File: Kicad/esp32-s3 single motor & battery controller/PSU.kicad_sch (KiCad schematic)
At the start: 73 parts, among them J5 Batt Balance connector, Q1 NMOS,12v, Q2 NMOS, 12v, Q3 NMOS,12v,PPak, Q4 NMOS, 12v, Q5 NMOS, 12v, Q7 NMOS,12v,PPak, U2 AP63203WU, U3 BQ76905RGRR, U4 BQ24780SRUYR

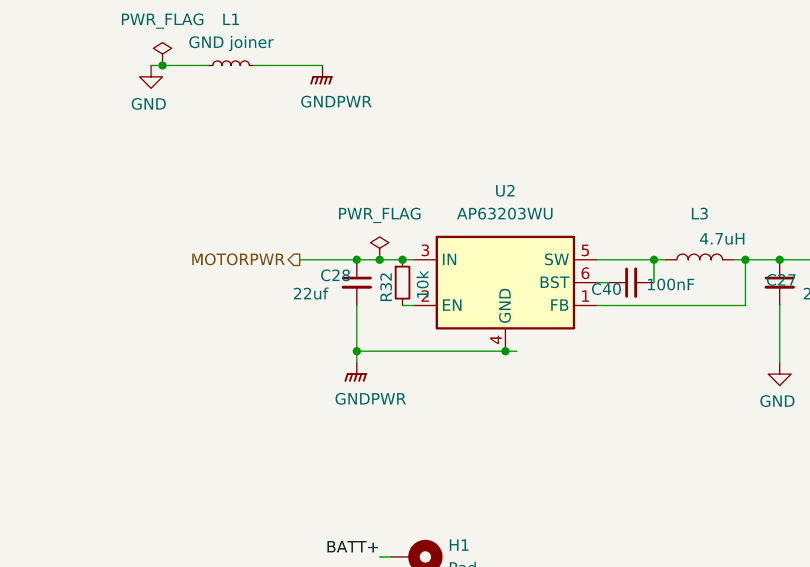
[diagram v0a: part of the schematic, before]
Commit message: Fixing routing issues after change
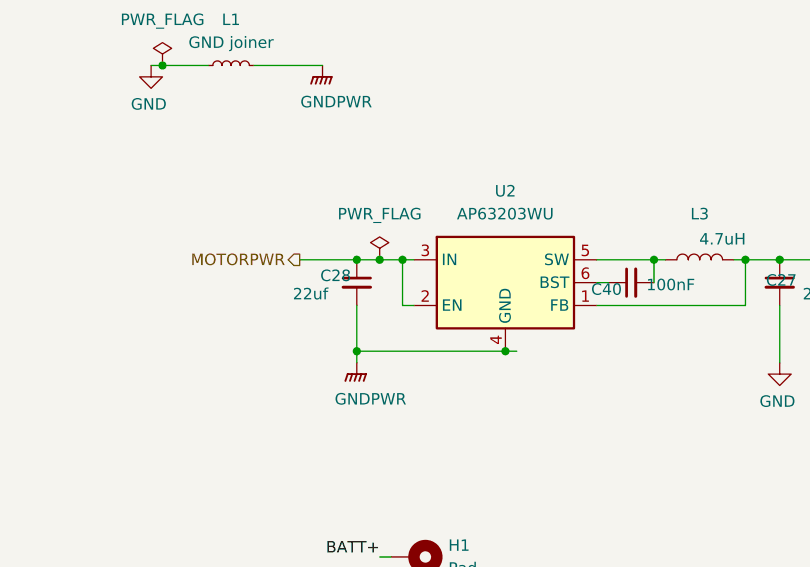
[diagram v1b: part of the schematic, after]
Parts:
- removed R32: 10k, Resistor_SMD:R_0603_1608Metric, symbol Device:R_Small
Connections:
- net MOTORPWR: now also U2.2 (EN)
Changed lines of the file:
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@@
 	)
 	(junction
-		(at 250.19 62.23)
-		(diameter 0)
-		(color 0 0 0 0)
-	)
-	(junction
 		(at 53.34 95.25)
 		(diameter 0)
@@
 	)
 	(junction
+		(at 250.19 62.23)
+		(diameter 0)
+		(color 0 0 0 0)
+	)
+	(junction
 		(at 261.62 72.39)
 		(diameter 0)
@@
 	(wire
 		(pts
+			(xy 250.19 62.23) (xy 251.46 62.23)
+		)
+		(stroke
+			(width 0)
+			(type default)
+		)
+	)
+	(wire
+		(pts
 			(xy 184.15 140.97) (xy 168.91 140.97)
 		)
@@
 	(wire
 		(pts
-			(xy 250.19 62.23) (xy 251.46 62.23)
+			(xy 247.65 62.23) (xy 250.19 62.23)
 		)
 		(stroke
@@
 	(wire
 		(pts
-			(xy 247.65 62.23) (xy 250.19 62.23)
+			(xy 53.34 105.41) (xy 49.53 105.41)
 		)
 		(stroke
@@
 	(wire
 		(pts
-			(xy 53.34 105.41) (xy 49.53 105.41)
+			(xy 53.34 123.19) (xy 19.05 123.19)
 		)
 		(stroke
@@
 	(wire
 		(pts
-			(xy 53.34 123.19) (xy 19.05 123.19)
+			(xy 101.6 118.11) (xy 106.68 118.11)
 		)
 		(stroke
@@
 	(wire
 		(pts
-			(xy 101.6 118.11) (xy 106.68 118.11)
+			(xy 184.15 125.73) (xy 184.15 128.27)
 		)
 		(stroke
@@
 	(wire
 		(pts
-			(xy 184.15 125.73) (xy 184.15 128.27)
+			(xy 95.25 76.2) (xy 97.79 76.2)
 		)
 		(stroke
@@
 	(wire
 		(pts
-			(xy 95.25 76.2) (xy 97.79 76.2)
+			(xy 44.45 128.27) (xy 53.34 128.27)
 		)
 		(stroke
@@
 	(wire
 		(pts
-			(xy 44.45 128.27) (xy 53.34 128.27)
+			(xy 166.37 170.18) (xy 163.83 170.18)
 		)
 		(stroke
@@
 	(wire
 		(pts
-			(xy 166.37 170.18) (xy 163.83 170.18)
+			(xy 250.19 62.23) (xy 250.19 67.31)
 		)
 		(stroke
@@
 					(unit 1)
 				)
-			)
-		)
-	)
-	(symbol
-		(lib_id "Device:R_Small")
-		(at 250.19 64.77 0)
-		(unit 1)
-		(exclude_from_sim no)
-		(in_bom yes)
-		(on_board yes)
-		(dnp no)
-		(property "Reference" "R32"
-			(at 248.412 65.278 90)
-			(effects
-				(font
-					(size 1.27 1.27)
-				)
-			)
-		)
-		(property "Value" "10k"
-			(at 252.476 65.024 90)
-			(effects
-				(font
-					(size 1.27 1.27)
-				)
-			)
-		)
-		(property "Footprint" "Resistor_SMD:R_0603_1608Metric"
-			(at 250.19 64.77 0)
-			(effects
-				(font
-					(size 1.27 1.27)
-				)
-				(hide yes)
-			)
-		)
-		(property "Datasheet" "~"
-			(at 250.19 64.77 0)
-			(effects
-				(font
-					(size 1.27 1.27)
-				)
-				(hide yes)
-			)
-		)
-		(property "Description" "Resistor, small symbol"
-			(at 250.19 64.77 0)
-			(effects
-				(font
-					(size 1.27 1.27)
-				)
-				(hide yes)
-			)
-		)
-		(pin "2"
-		)
-		(pin "1"
-		)
-		(instances
-			(project "esp32-s3 single motor & battery controller"
-				(path "/eb3f183d-8bb1-43a5-a363-092ed67891e3/a57a0b4f-e246-497c-8d94-688647d8fd03"
-					(reference "R32")
-					(unit 1)
-				)

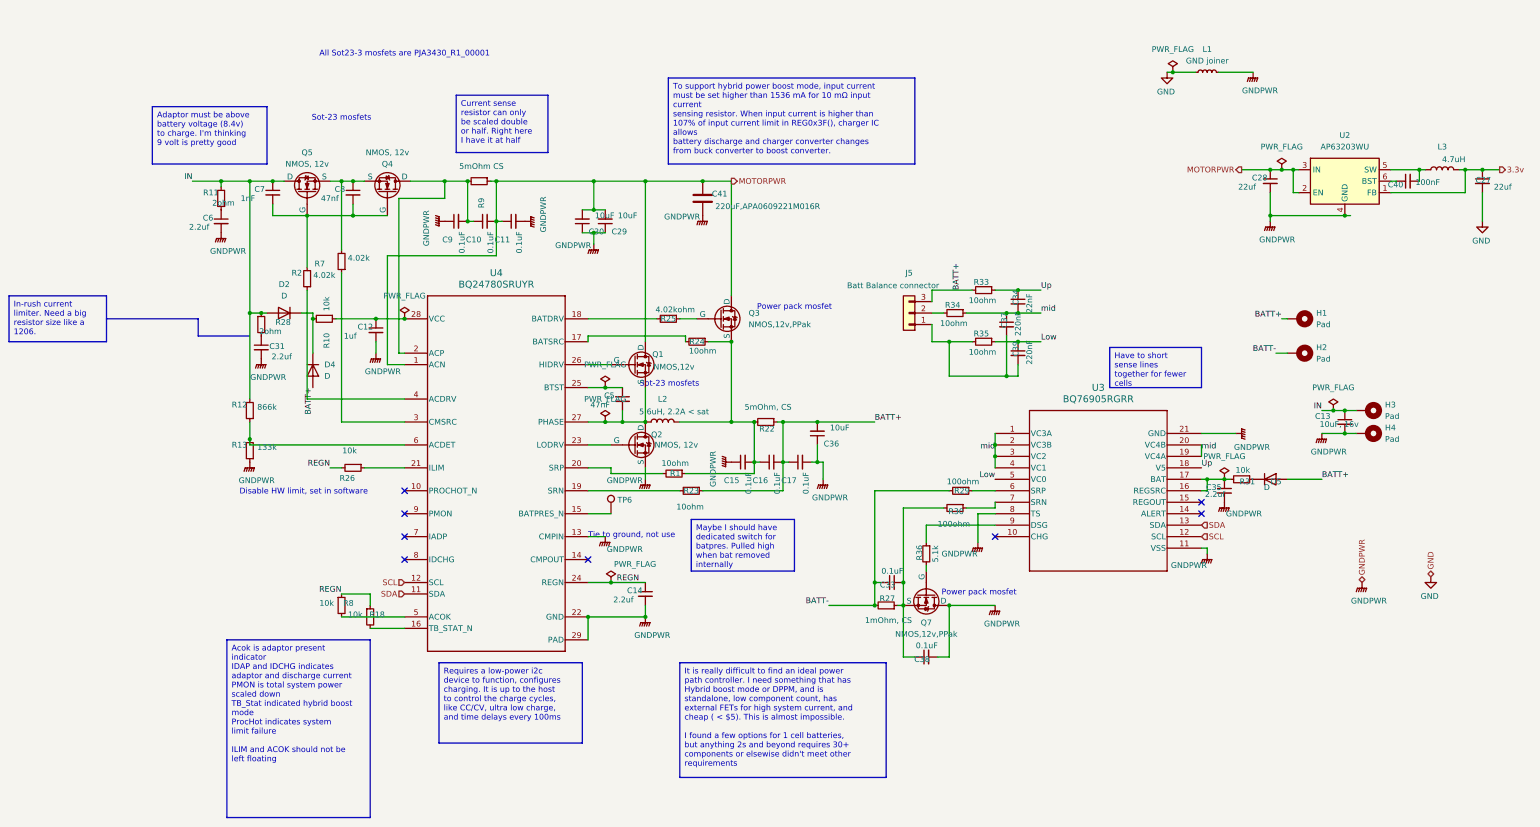
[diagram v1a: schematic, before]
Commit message: Finished design
I speced out the proper diodes, routed the wires away from the inductor, added more ground vias, and did some general cleanup.
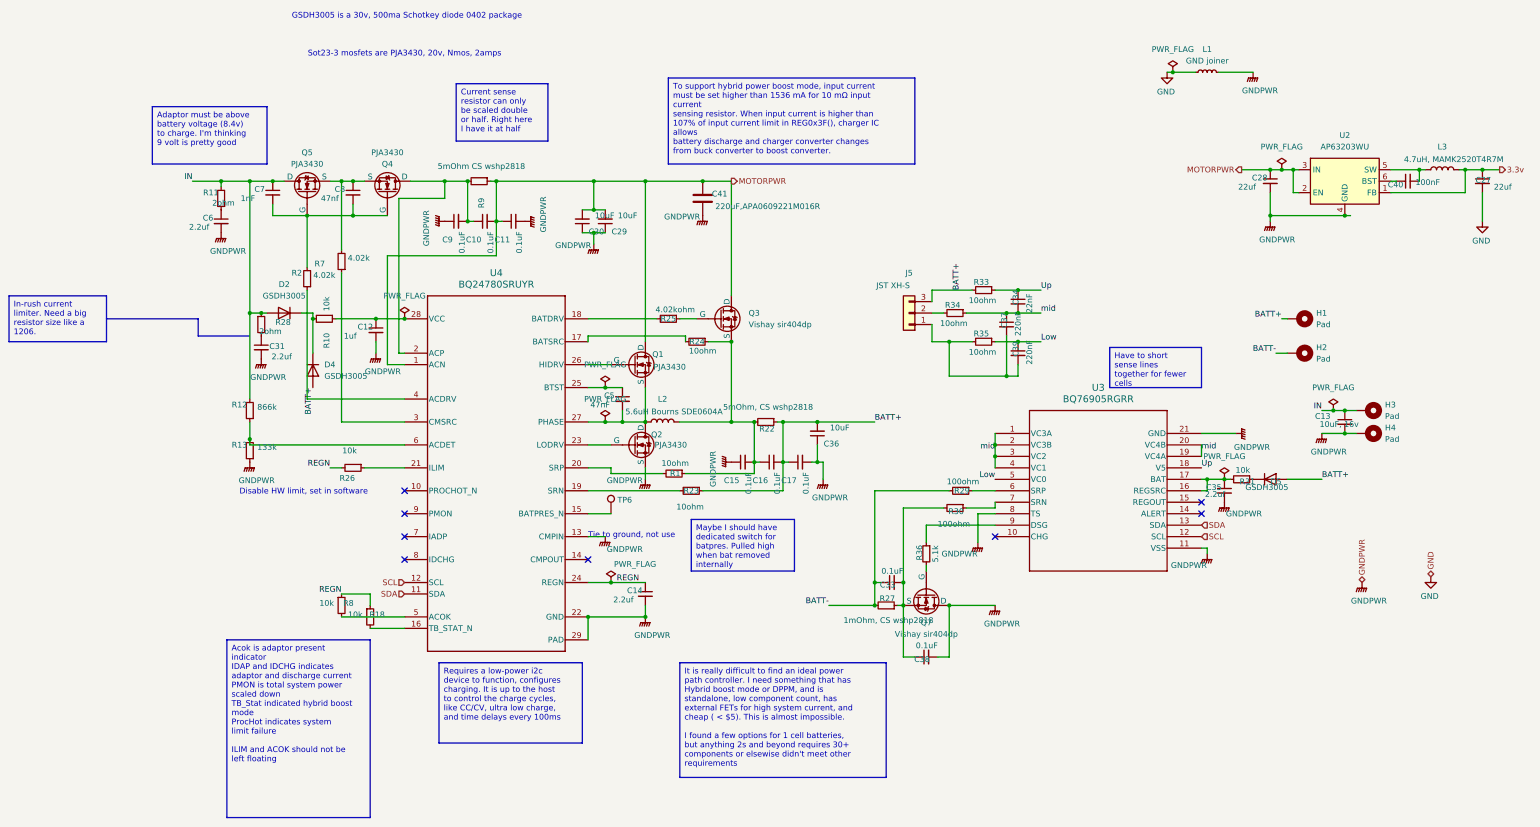
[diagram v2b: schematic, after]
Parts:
- D2, D4, D5: value D -> GSDH3005; footprint Diode_SMD:D_0603_1608Metric -> Diode_SMD:D_0402_1005Metric
- J5: value Batt Balance connector -> JST XH-S
- L2: value 5.6uH, 2.2A < sat -> 5.6uH Bourns SDE0604A
- L3: value 4.7uH -> 4.7uH, MAMK2520T4R7M
- Q1: value NMOS,12v -> PJA3430
- Q2, Q4, Q5: value NMOS, 12v -> PJA3430
- Q3, Q7: value NMOS,12v,PPak -> Vishay sir404dp
- R22: value 5mOhm, CS -> 5mOhm, CS wshp2818
- R27: value 1mOhm, CS -> 1mOhm, CS wshp2818
- R9: value 5mOhm CS -> 5mOhm CS wshp2818
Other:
- note added: "GSDH3005 is a 30v, 500ma Schotkey diode 0402 package"
- note added: "Sot23-3 mosfets are PJA3430, 20v, Nmos, 2amps"
- note removed: "All Sot23-3 mosfets are PJA3430_R1_00001"
- note removed: "Power pack mosfet"
- note removed: "Sot-23 mosfets"
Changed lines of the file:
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@@
 	(text_box "Current sense resistor can only be scaled double or half. Right here I have it at half"
 		(exclude_from_sim no)
-		(at 64.77 45.72 0)
+		(at 64.77 43.18 0)
 		(size 20.32 12.7)
 		(stroke
@@
 		)
 	)
-	(text "Sot-23 mosfets"
-		(exclude_from_sim no)
-		(at 39.37 50.8 0)
-		(effects
-			(font
-				(size 1.27 1.27)
-			)
-		)
-	)
-	(text "Sot-23 mosfets"
-		(exclude_from_sim no)
-		(at 112.014 109.728 0)
-		(effects
-			(font
-				(size 1.27 1.27)
-			)
-		)
-	)
-	(text "All Sot23-3 mosfets are PJA3430_R1_00001"
+	(text "Sot23-3 mosfets are PJA3430, 20v, Nmos, 2amps"
 		(exclude_from_sim no)
 		(at 53.34 36.576 0)
@@
 		)
 	)
-	(text "Power pack mosfet"
-		(exclude_from_sim no)
-		(at 180.594 155.956 0)
-		(effects
-			(font
-				(size 1.27 1.27)
-			)
-		)
-	)
-	(text "Power pack mosfet"
+	(text "GSDH3005 is a 30v, 500ma Schotkey diode 0402 package"
 		(exclude_from_sim no)
-		(at 139.7 92.71 0)
+		(at 53.848 28.194 0)
 		(effects
 			(font
@@
 			)
 		)
-		(property "Value" "D"
+		(property "Value" "GSDH3005"
 			(at 244.348 132.588 0)
 			(effects
@@
 			)
 		)
-		(property "Footprint" "Diode_SMD:D_0603_1608Metric"
+		(property "Footprint" "Diode_SMD:D_0402_1005Metric"
 			(at 245.11 130.81 0)
 			(effects
@@
 			)
 		)
-		(property "Value" "NMOS, 12v"
+		(property "Value" "PJA3430"
 			(at 49.53 58.42 90)
 			(effects
@@
 			)
 		)
-		(property "Value" "4.7uH"
+		(property "Value" "4.7uH, MAMK2520T4R7M"
 			(at 285.75 59.944 90)
 			(effects
@@
 			)
 		)
-		(property "Value" "1mOhm, CS"
+		(property "Value" "1mOhm, CS wshp2818"
 			(at 160.528 162.052 90)
 			(effects
@@
 			)
 		)
-		(property "Value" "D"
+		(property "Value" "GSDH3005"
 			(at 35.56 107.9499 90)
 			(effects
@@
 			)
 		)
-		(property "Footprint" "Diode_SMD:D_0603_1608Metric"
+		(property "Footprint" "Diode_SMD:D_0402_1005Metric"
 			(at 33.02 106.68 0)
 			(effects
@@
 			)
 		)
-		(property "Value" "5mOhm CS"
+		(property "Value" "5mOhm CS wshp2818"
 			(at 70.358 61.468 90)
 			(effects
@@
 			)
 		)
-		(property "Value" "Batt Balance connector"
+		(property "Value" "JST XH-S"
 			(at 161.544 87.884 0)
 			(effects
@@
 			)
 		)
-		(property "Value" "5mOhm, CS"
+		(property "Value" "5mOhm, CS wshp2818"
 			(at 133.858 114.808 90)
 			(effects
@@
 			)
 		)
-		(property "Value" "NMOS,12v,PPak"
+		(property "Value" "Vishay sir404dp"
 			(at 168.91 165.1 90)
 			(effects
@@
 			)
 		)
-		(property "Value" "5.6uH, 2.2A < sat"
+		(property "Value" "5.6uH Bourns SDE0604A"
 			(at 113.03 115.824 90)
 			(effects
@@
 			)
 		)
-		(property "Value" "NMOS, 12v"
+		(property "Value" "PJA3430"
 			(at 108.712 123.19 0)
 			(effects
@@
 			)
 		)
-		(property "Value" "NMOS,12v,PPak"
+		(property "Value" "Vishay sir404dp"
 			(at 129.54 96.5199 0)
 			(effects
@@
 			)
 		)
-		(property "Value" "NMOS, 12v"
+		(property "Value" "PJA3430"
 			(at 31.75 60.96 90)
 			(effects
@@
 			)
 		)
-		(property "Value" "D"
+		(property "Value" "GSDH3005"
 			(at 26.67 90.17 0)
 			(effects
@@
 			)
 		)
-		(property "Footprint" "Diode_SMD:D_0603_1608Metric"
+		(property "Footprint" "Diode_SMD:D_0402_1005Metric"
 			(at 26.67 93.98 0)
 			(effects
@@
 			)
 		)
-		(property "Value" "NMOS,12v"
+		(property "Value" "PJA3430"
 			(at 108.458 105.918 0)
 			(effects
